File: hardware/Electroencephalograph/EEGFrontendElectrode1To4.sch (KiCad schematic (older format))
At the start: 81 parts, among them J1 Conn_01x08_Male

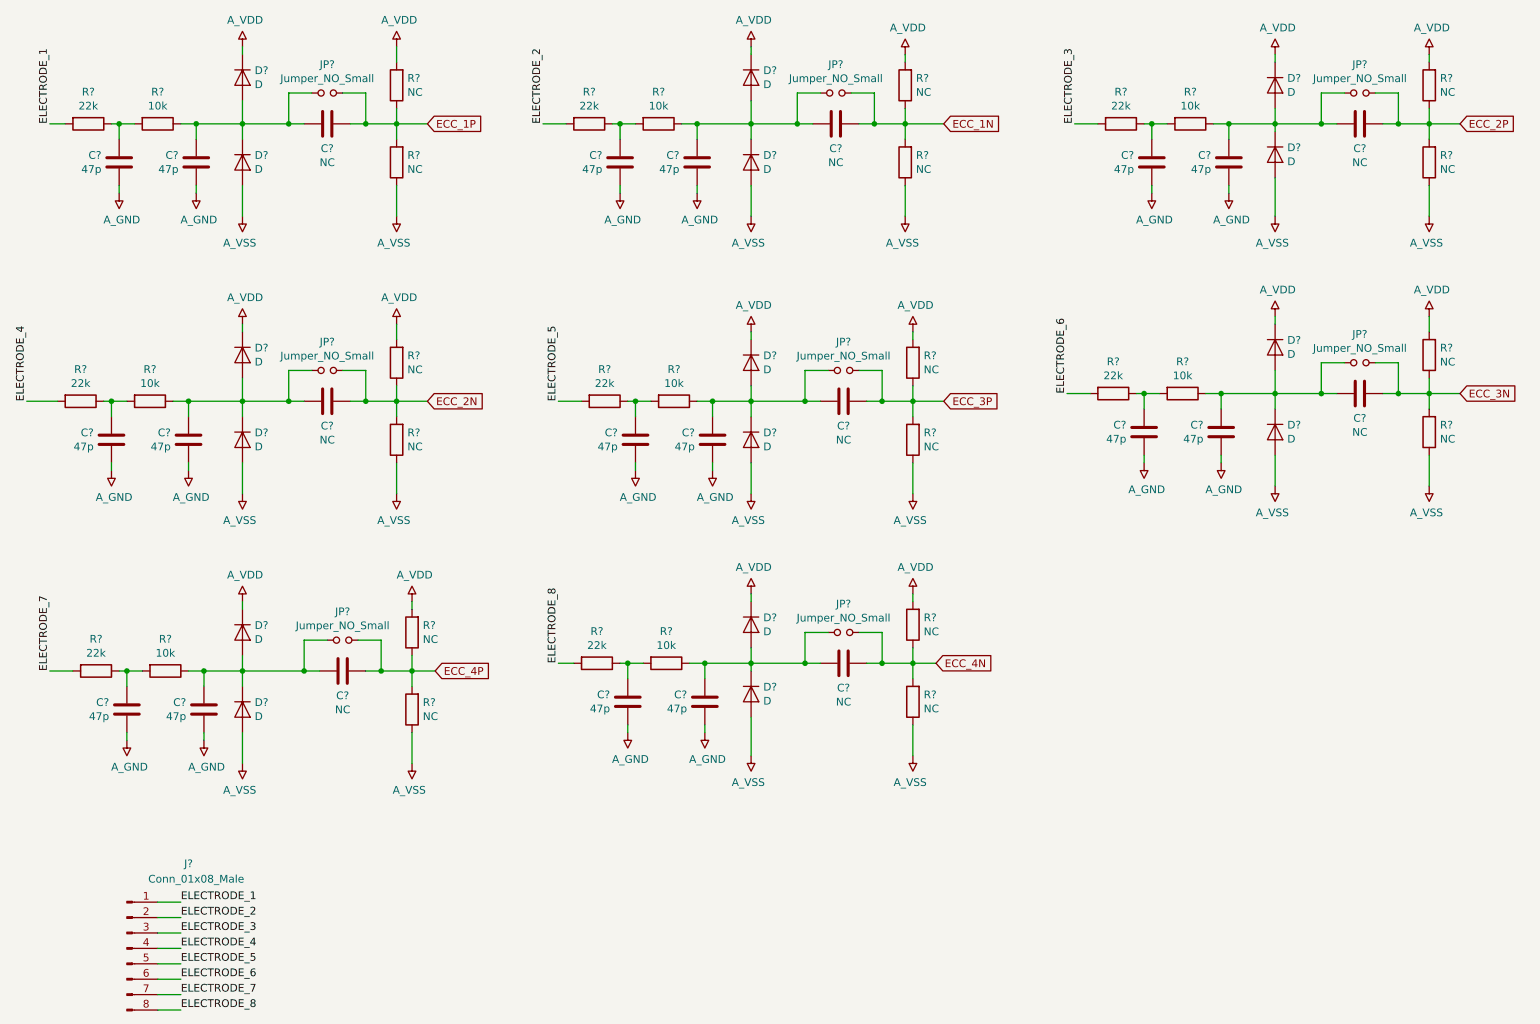
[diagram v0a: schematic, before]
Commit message: fixed power supply symbols
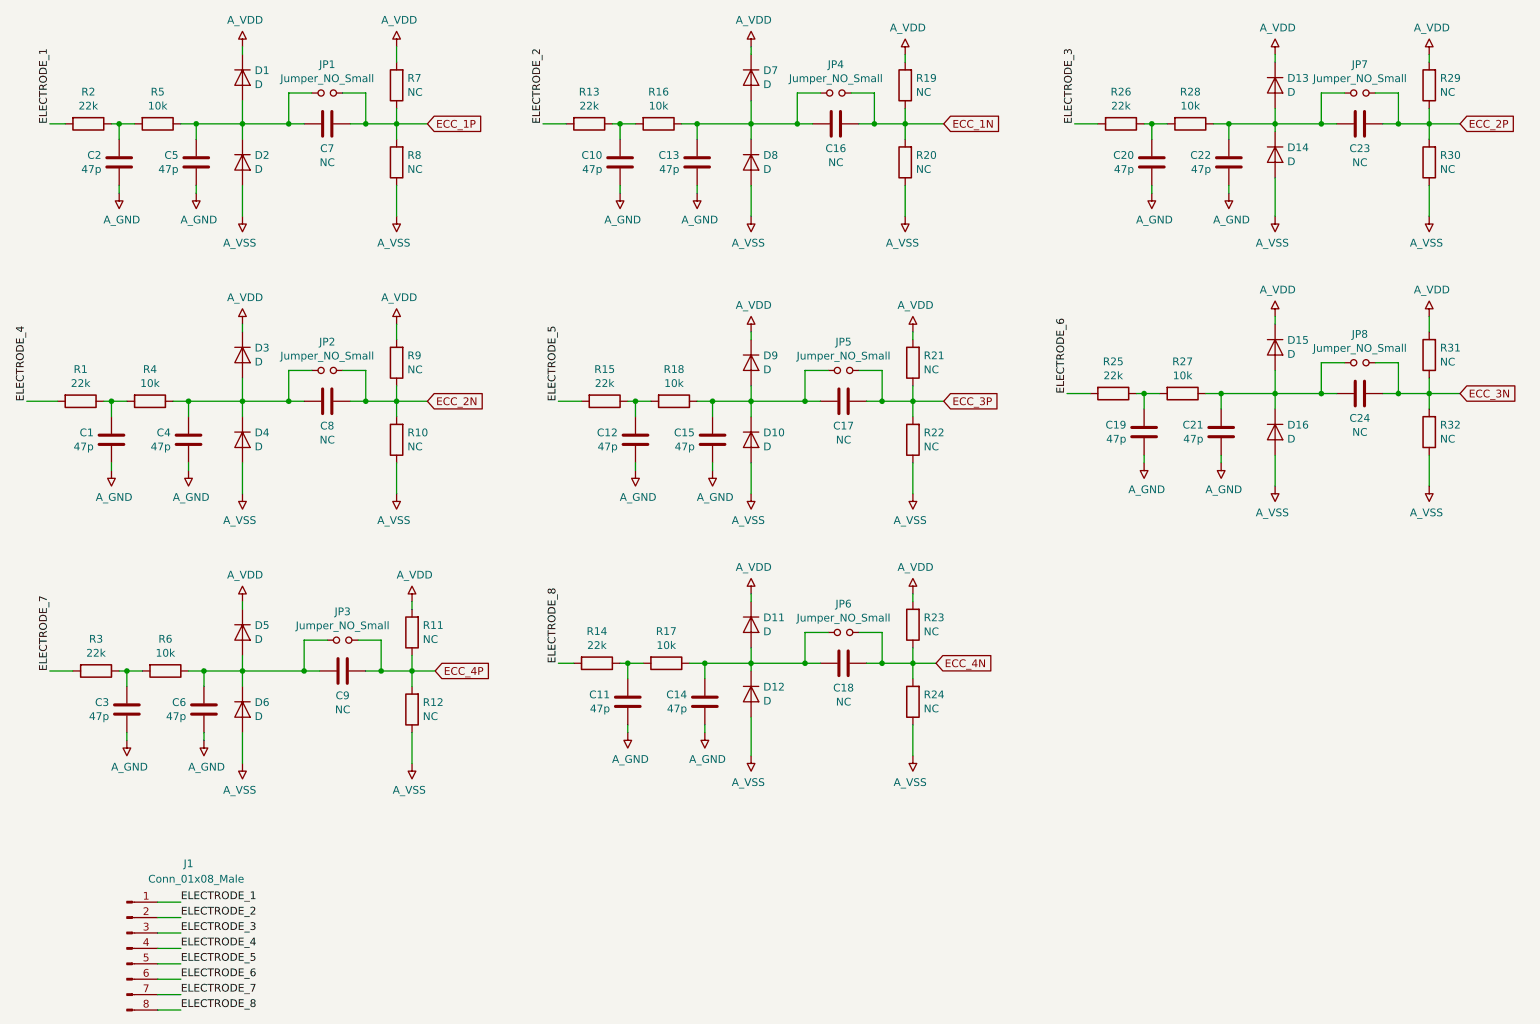
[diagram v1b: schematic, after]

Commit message: placing components groups
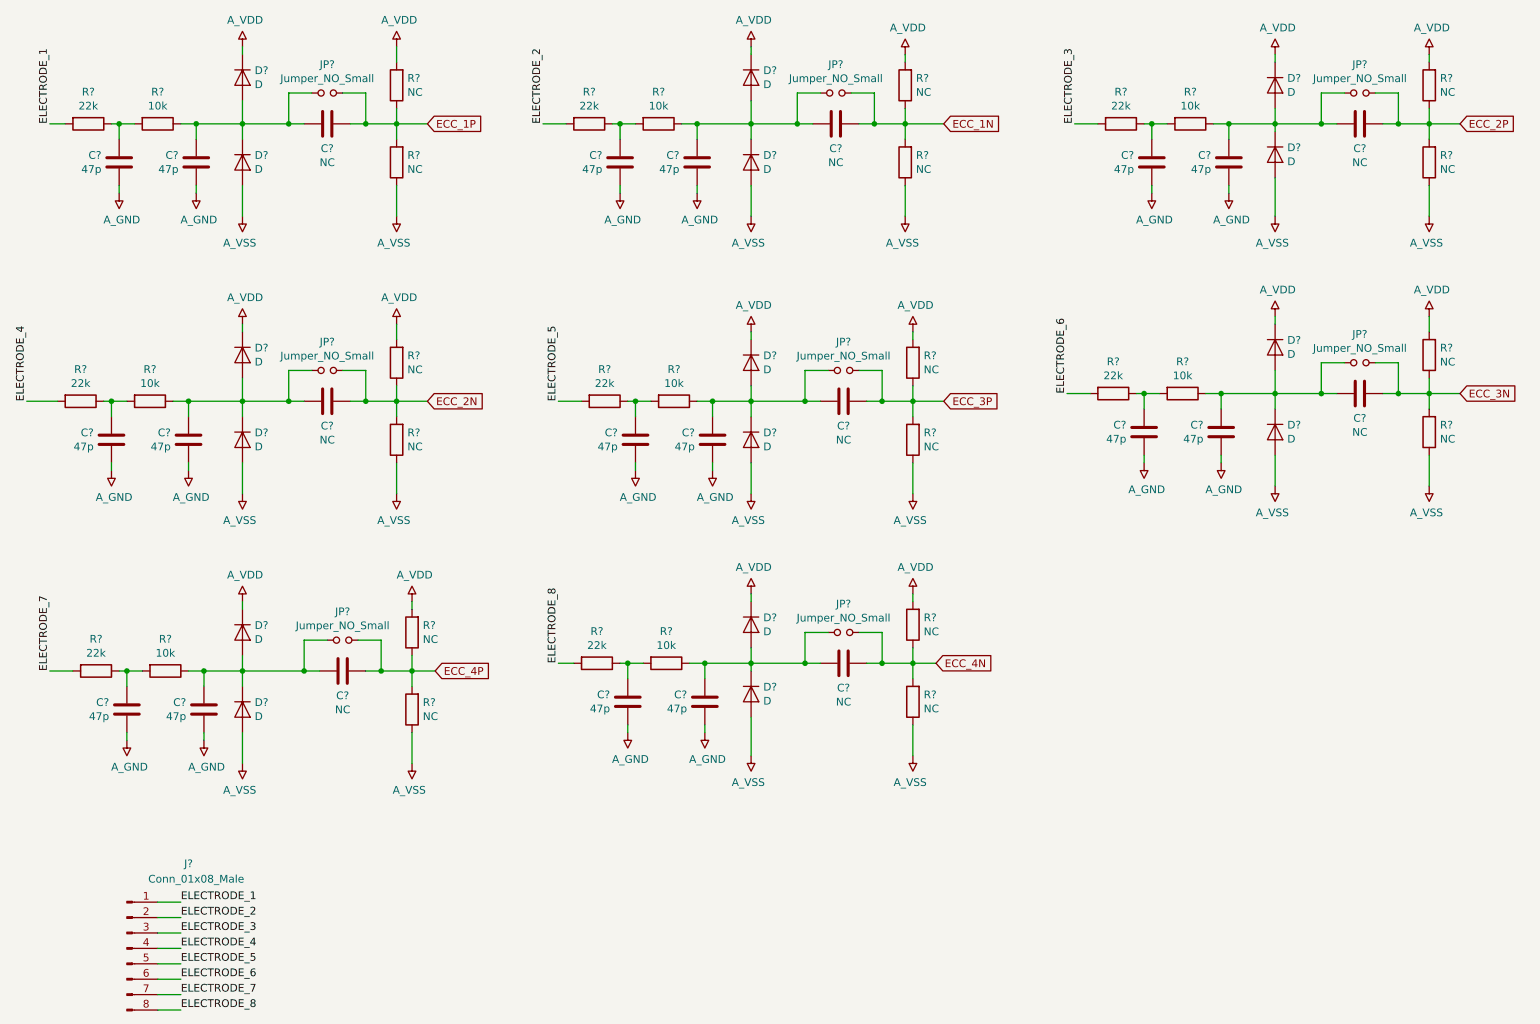
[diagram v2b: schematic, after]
